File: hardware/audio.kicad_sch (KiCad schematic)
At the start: 6 parts, among them U8 PCM5102A

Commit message: TX Filter pt. 2
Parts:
- added C24: 10nF, symbol Device:C
- added C25: 100nF, symbol Device:C
- added R5: 47k, symbol Device:R
- added R6: 470, symbol Device:R
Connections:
- net GND: now also C19.2, C20.2, C24.2
- net at U8.6 (OUTL): now also R5.1
- new net: C25.1, R6.2
- new net: C24.1, R5.2, R6.1
- new net MIC+: C25.2

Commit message: RX Filter
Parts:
- added C26: 1uF, symbol Device:C
- added C27: 4.7nF, symbol Device:C
- added R10, R9: 47k, symbol Device:R
- added R7, R8: 4.7k, symbol Device:R
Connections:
- net +3.3V: now also R9.1
- net GND: now also C27.2, R10.2
- new net: C27.1, R7.2, R8.1
- new net: C26.2, R7.1
- new net RX_AUDIO: R10.1, R8.2, R9.2
- new net SPK+: C26.1

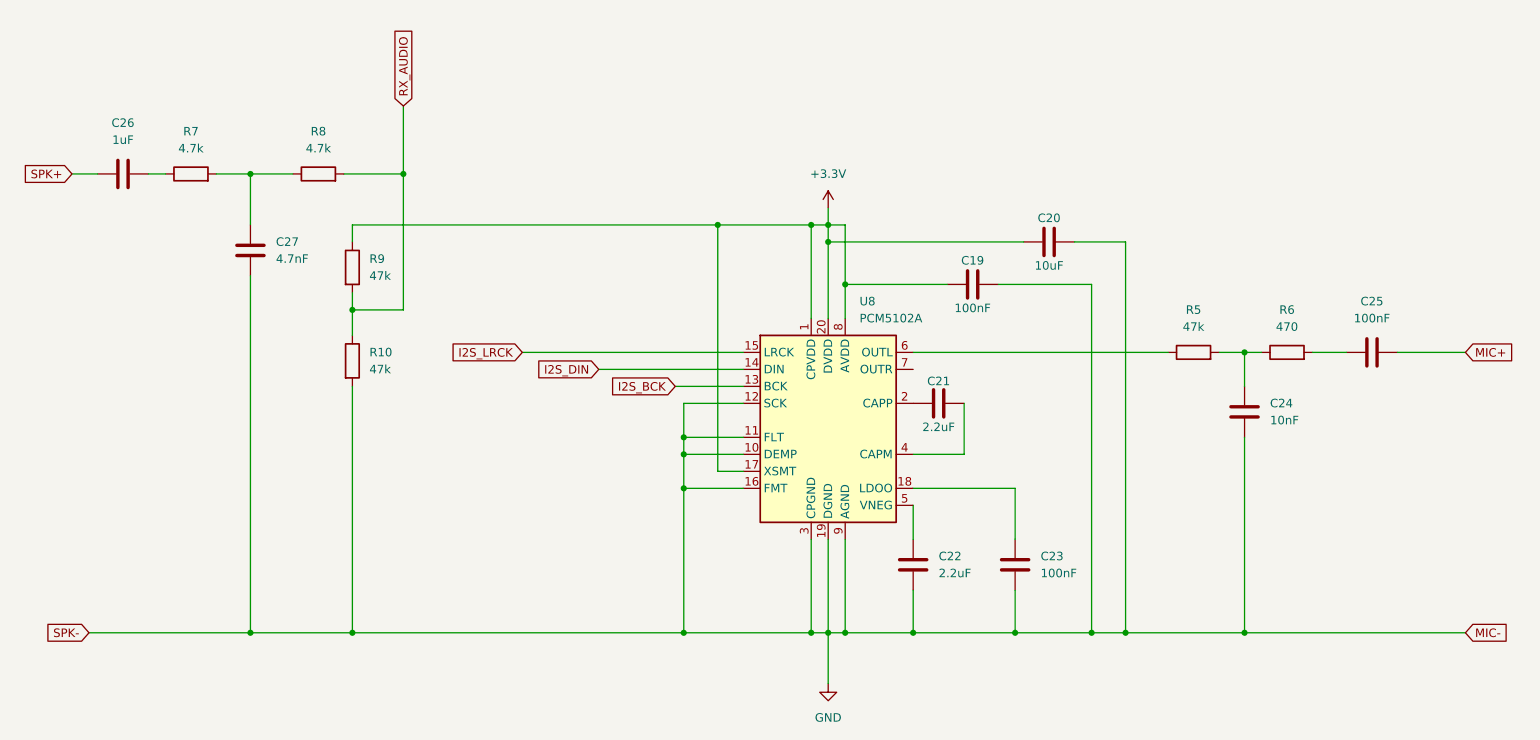
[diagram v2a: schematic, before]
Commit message: all design sheets complete, ERC clean
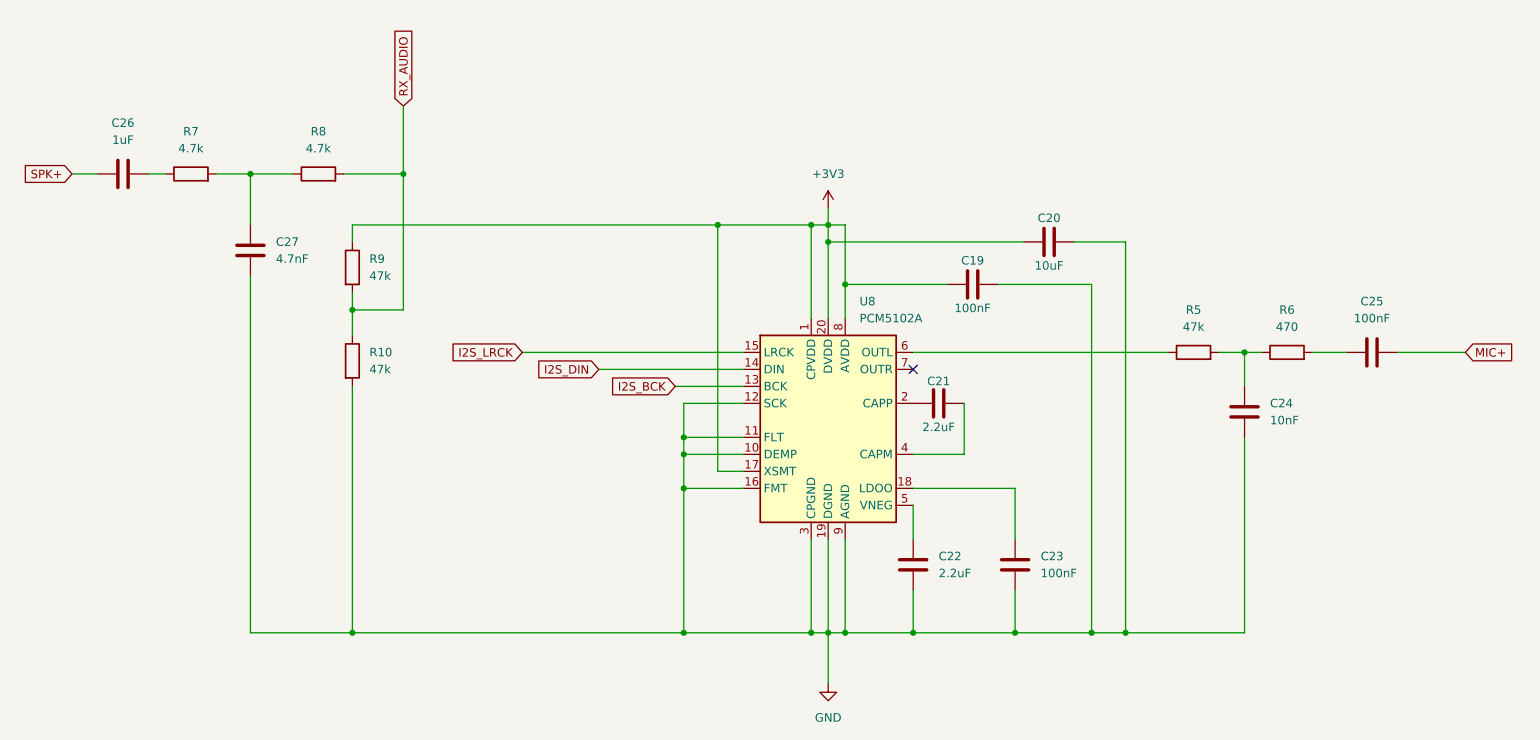
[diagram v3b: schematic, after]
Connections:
- net +3.3V renamed +3V3
- no-connect marks 0 -> 1
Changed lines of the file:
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@@
-	)
-	(junction
-		(at 60.96 120.65)
-		(diameter 0)
-		(color 0 0 0 0)
 	)
 	(junction
@@
 	)
 	(junction
-		(at 209.55 120.65)
-		(diameter 0)
-		(color 0 0 0 0)
-	)
-	(junction
 		(at 60.96 52.07)
 		(diameter 0)
@@
 	)
 	(junction
+		(at 83.82 52.07)
+		(diameter 0)
+		(color 0 0 0 0)
+	)
+	(junction
+		(at 130.81 59.69)
+		(diameter 0)
+		(color 0 0 0 0)
+	)
+	(junction
+		(at 149.86 120.65)
+		(diameter 0)
+		(color 0 0 0 0)
+	)
+	(junction
+		(at 144.78 59.69)
+		(diameter 0)
+		(color 0 0 0 0)
+	)
+	(junction
 		(at 209.55 78.74)
 		(diameter 0)
@@
 	)
 	(junction
-		(at 83.82 52.07)
-		(diameter 0)
-		(color 0 0 0 0)
-	)
-	(junction
-		(at 130.81 59.69)
-		(diameter 0)
-		(color 0 0 0 0)
-	)
-	(junction
-		(at 149.86 120.65)
-		(diameter 0)
-		(color 0 0 0 0)
-	)
-	(junction
-		(at 144.78 59.69)
-		(diameter 0)
-		(color 0 0 0 0)
-	)
-	(junction
 		(at 125.73 99.06)
 		(diameter 0)
@@
 		(color 0 0 0 0)
 	)
+	(no_connect
+		(at 160.02 81.28)
+	)
 	(wire
 		(pts
@@
 	(wire
 		(pts
+			(xy 209.55 78.74) (xy 209.55 83.82)
+		)
+		(stroke
+			(width 0)
+			(type default)
+		)
+	)
+	(wire
+		(pts
 			(xy 83.82 41.91) (xy 83.82 52.07)
 		)
@@
 	(wire
 		(pts
-			(xy 209.55 120.65) (xy 242.57 120.65)
-		)
-		(stroke
-			(width 0)
-			(type default)
-		)
-	)
-	(wire
-		(pts
 			(xy 125.73 93.98) (xy 125.73 99.06)
 		)
@@
 	(wire
 		(pts
+			(xy 209.55 78.74) (xy 212.09 78.74)
+		)
+		(stroke
+			(width 0)
+			(type default)
+		)
+	)
+	(wire
+		(pts
 			(xy 134.62 86.36) (xy 125.73 86.36)
 		)
@@
 	(wire
 		(pts
-			(xy 209.55 78.74) (xy 212.09 78.74)
+			(xy 205.74 78.74) (xy 209.55 78.74)
 		)
 		(stroke
@@
 	(wire
 		(pts
-			(xy 36.83 120.65) (xy 60.96 120.65)
-		)
-		(stroke
-			(width 0)
-			(type default)
-		)
-	)
-	(wire
-		(pts
 			(xy 130.81 59.69) (xy 130.81 96.52)
 		)
@@
 	(wire
 		(pts
-			(xy 209.55 78.74) (xy 209.55 83.82)
-		)
-		(stroke
-			(width 0)
-			(type default)
-		)
-	)
-	(wire
-		(pts
 			(xy 76.2 59.69) (xy 76.2 62.23)
 		)
@@
 			(width 0)
 			(type default)
-		)
-	)
-	(wire
-		(pts
-			(xy 205.74 78.74) (xy 209.55 78.74)
-		)
-		(stroke
-			(width 0)
-			(type default)
-		)
-	)
-	(global_label "MIC-"
-		(shape input)
-		(at 242.57 120.65 0)
-		(fields_autoplaced yes)
-		(effects
-			(font
-				(size 1.27 1.27)
-			)
-			(justify left)
-		)
-		(property "Intersheetrefs" "${INTERSHEET_REFS}"
-			(at 250.4538 120.65 0)
-			(effects
-				(font
-					(size 1.27 1.27)
-				)
-				(justify left)
-				(hide yes)
-			)
 		)
 	)
@@
 		)
 	)
-	(global_label "SPK-"
-		(shape input)
-		(at 36.83 120.65 180)
-		(fields_autoplaced yes)
-		(effects
-			(font
-				(size 1.27 1.27)
-			)
-			(justify right)
-		)
-		(property "Intersheetrefs" "${INTERSHEET_REFS}"
-			(at 28.5229 120.65 0)
-			(effects
-				(font
-					(size 1.27 1.27)
-				)
-				(justify right)
-				(hide yes)
-			)
-		)
-	)
 	(global_label "I2S_BCK"
 		(shape input)
@@
 				(justify right)
 				(hide yes)
-			)
-		)
-	)
-	(symbol
-		(lib_id "power:+3.3V")
-		(at 147.32 57.15 0)
-		(unit 1)
-		(exclude_from_sim no)
-		(in_bom yes)
-		(on_board yes)
-		(dnp no)
-		(fields_autoplaced yes)
-		(property "Reference" "#PWR05"
-			(at 147.32 60.96 0)
-			(effects
-				(font
-					(size 1.27 1.27)
-				)
-				(hide yes)
-			)
-		)
-		(property "Value" "+3.3V"
-			(at 147.32 52.07 0)
-			(effects
-				(font
-					(size 1.27 1.27)
-				)
-			)
-		)
-		(property "Footprint" ""
-			(at 147.32 57.15 0)
-			(effects
-				(font
-					(size 1.27 1.27)
-				)
-				(hide yes)
-			)
-		)
-		(property "Datasheet" ""
-			(at 147.32 57.15 0)
-			(effects
-				(font
-					(size 1.27 1.27)
-				)
-				(hide yes)
-			)
-		)
-		(property "Description" "Power symbol creates a global label with name \"+3.3V\""
-			(at 147.32 57.15 0)
-			(effects
-				(font
-					(size 1.27 1.27)
-				)
-				(hide yes)
-			)
-		)
-		(pin "1"
-		)
-		(instances
-			(project ""
-				(path "/6bfeada4-0da3-4bdd-af4a-70929e466b35/93aa96ae-ec45-4b38-a4d0-fe0c2fa30fed"
-					(reference "#PWR05")
-					(unit 1)
-				)
 			)
 		)
@@
 					(unit 1)
 				)
+			)
+		)
+	)
+	(symbol
+		(lib_id "power:+3V3")
+		(at 147.32 57.15 0)
+		(unit 1)
+		(exclude_from_sim no)
+		(in_bom yes)
+		(on_board yes)
+		(dnp no)
+		(fields_autoplaced yes)
+		(property "Reference" "#PWR05"
+			(at 147.32 60.96 0)
+			(effects
+				(font
+					(size 1.27 1.27)
+				)
+				(hide yes)
+			)
+		)
+		(property "Value" "+3V3"
+			(at 147.32 52.07 0)
+			(effects
+				(font
+					(size 1.27 1.27)
+				)
+			)
+		)
+		(property "Footprint" ""
+			(at 147.32 57.15 0)
+			(effects
+				(font
+					(size 1.27 1.27)
+				)
+				(hide yes)
+			)
+		)
+		(property "Datasheet" ""
+			(at 147.32 57.15 0)
+			(effects
+				(font
+					(size 1.27 1.27)
+				)
+				(hide yes)
+			)
+		)
+		(property "Description" "Power symbol creates a global label with name \"+3V3\""
+			(at 147.32 57.15 0)
+			(effects
+				(font
+					(size 1.27 1.27)
+				)
+				(hide yes)
+			)
+		)
+		(pin "1"
+		)
+		(instances
+			(project ""
+				(path "/6bfeada4-0da3-4bdd-af4a-70929e466b35/93aa96ae-ec45-4b38-a4d0-fe0c2fa30fed"
+					(reference "#PWR05")
+					(unit 1)
+				)
